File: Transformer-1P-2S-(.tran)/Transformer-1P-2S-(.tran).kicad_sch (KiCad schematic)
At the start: 9 parts

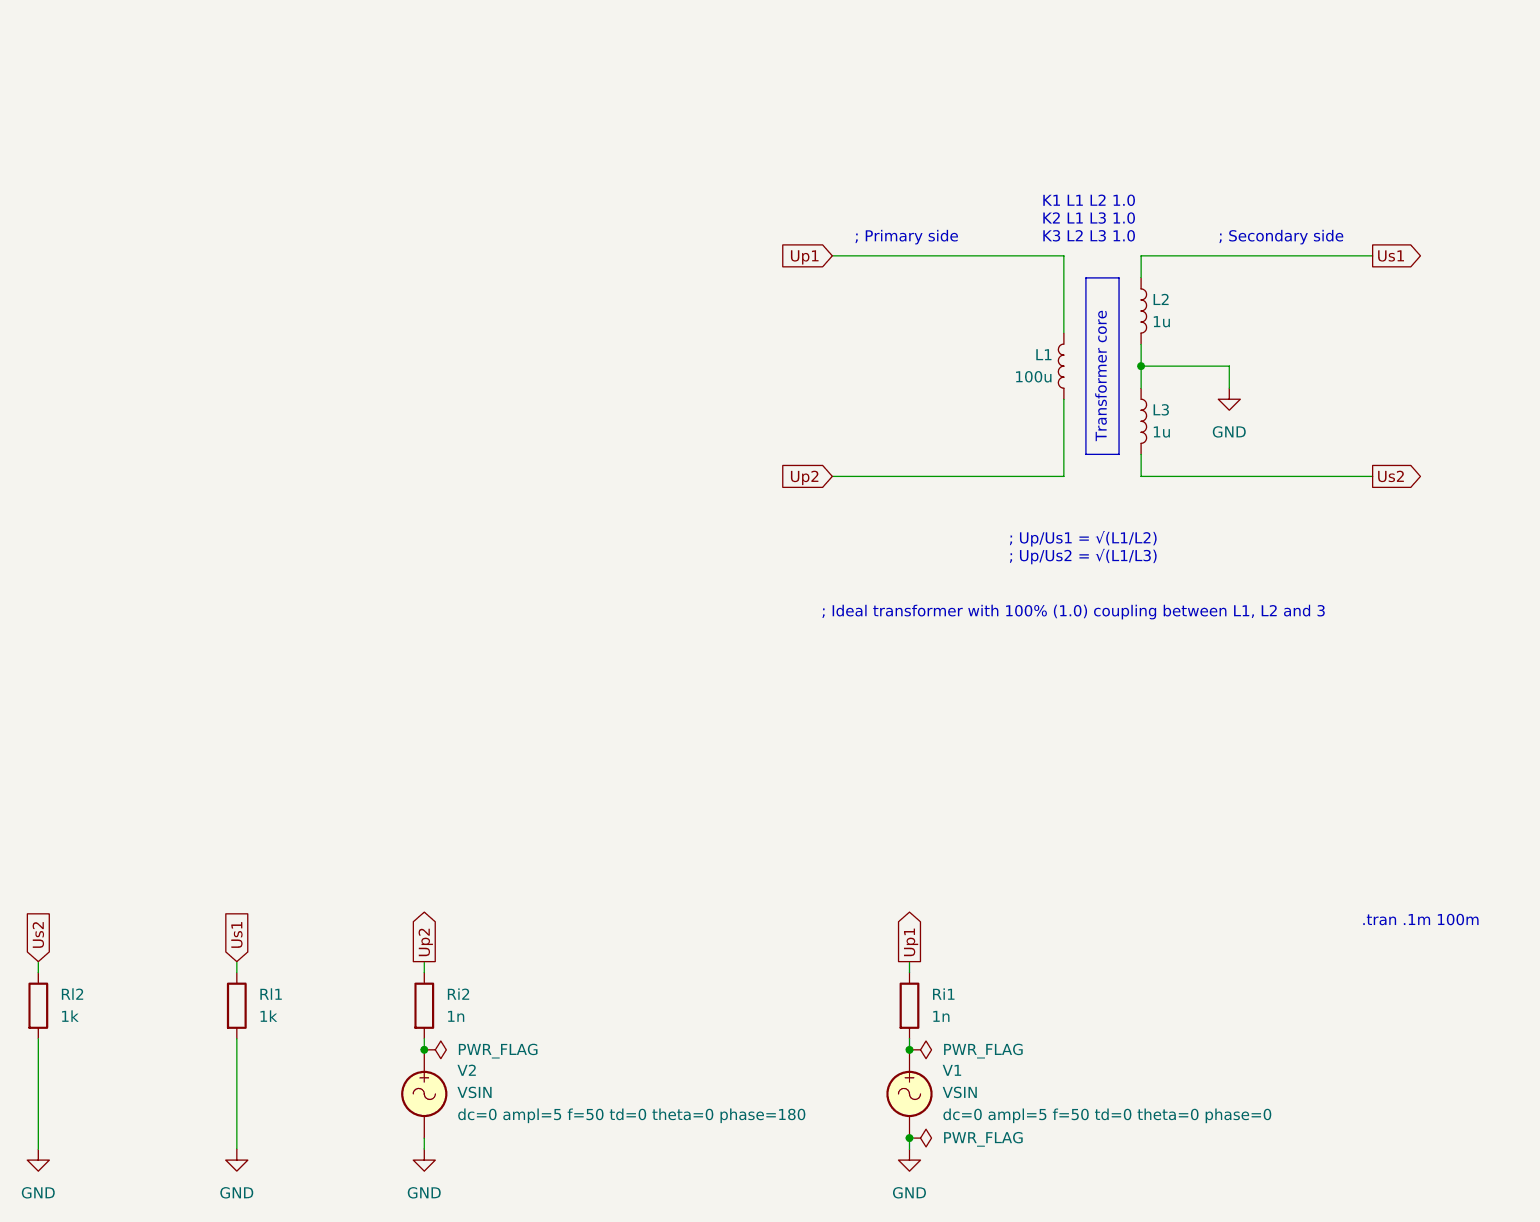
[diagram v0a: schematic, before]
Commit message: Updated all schematics and prepared for KiCad 8.0
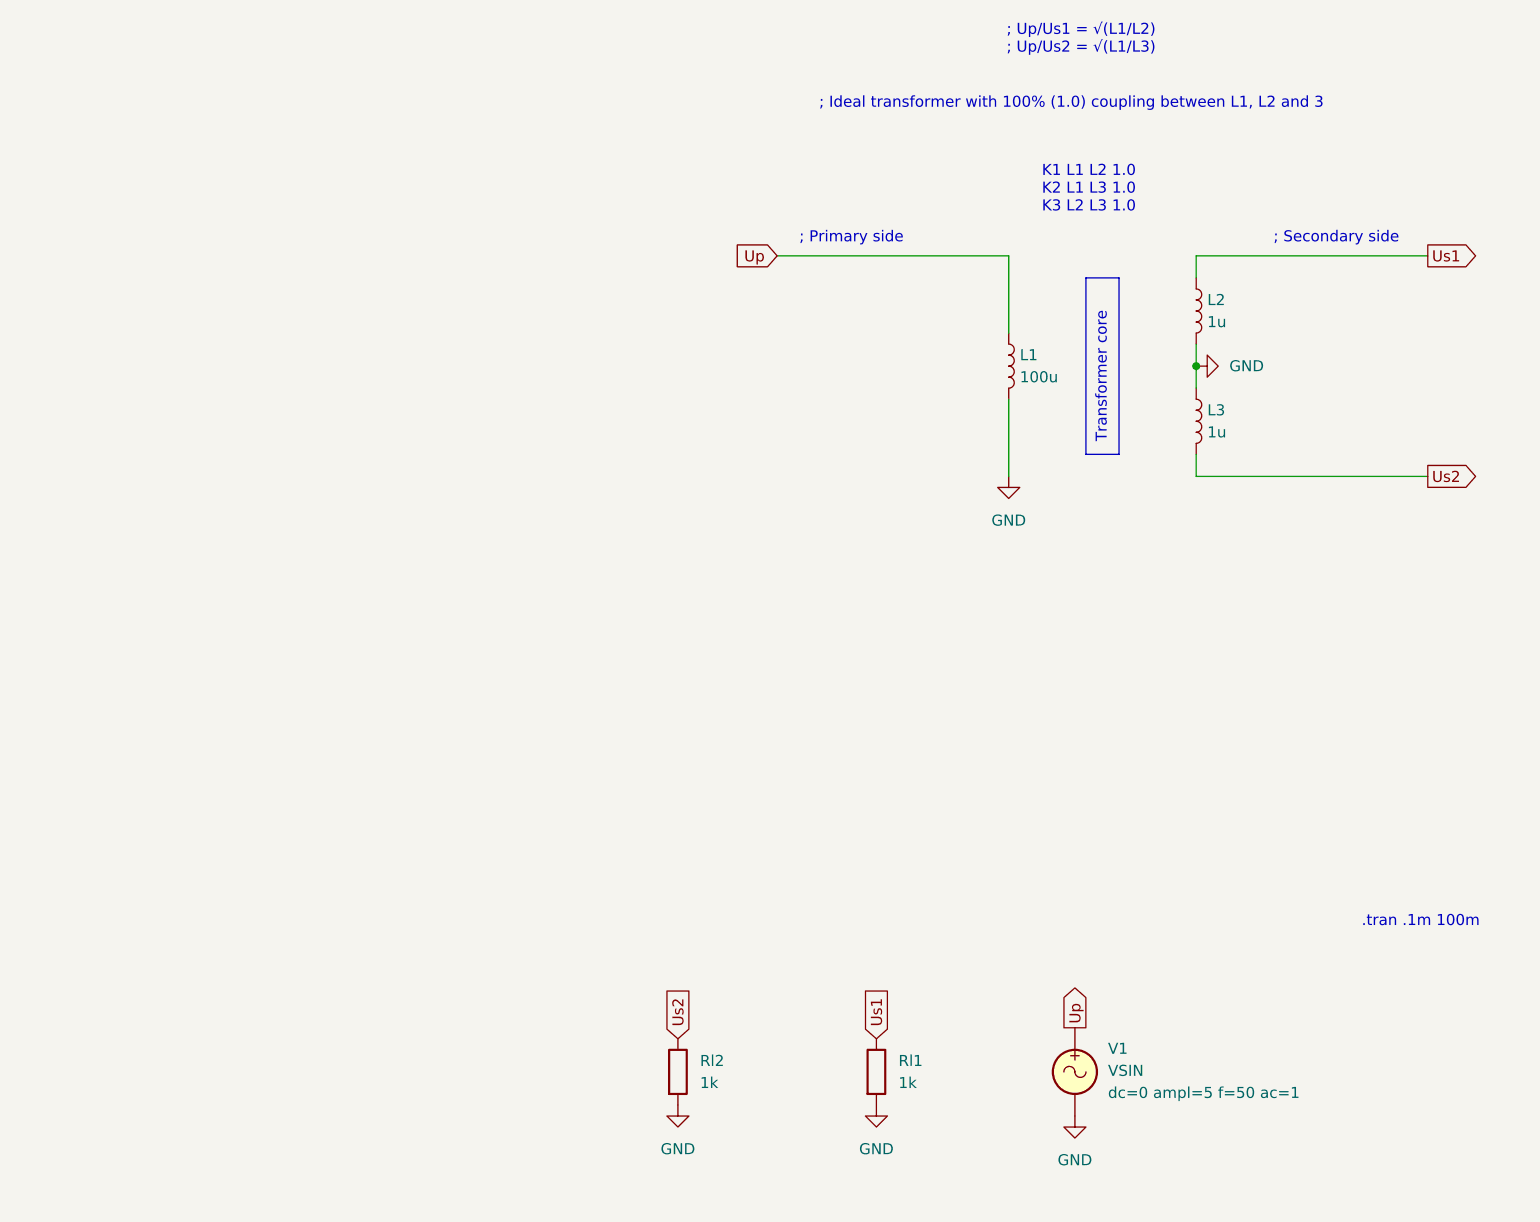
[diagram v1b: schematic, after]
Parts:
- removed Ri1, Ri2: 1n, symbol Device:R
- removed V2: VSIN, symbol Simulation_SPICE:VSIN
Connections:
- net Up1 is gone; now on net Up: L1.1
- net Up2 is gone; now on net GND: L1.2
- net Up: now reaches V1.1
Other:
- moved on the sheet: Rl1, Rl2
